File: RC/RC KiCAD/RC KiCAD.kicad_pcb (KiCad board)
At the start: 2 copper layers, 15 parts, among them U1 TL431AIDBZR

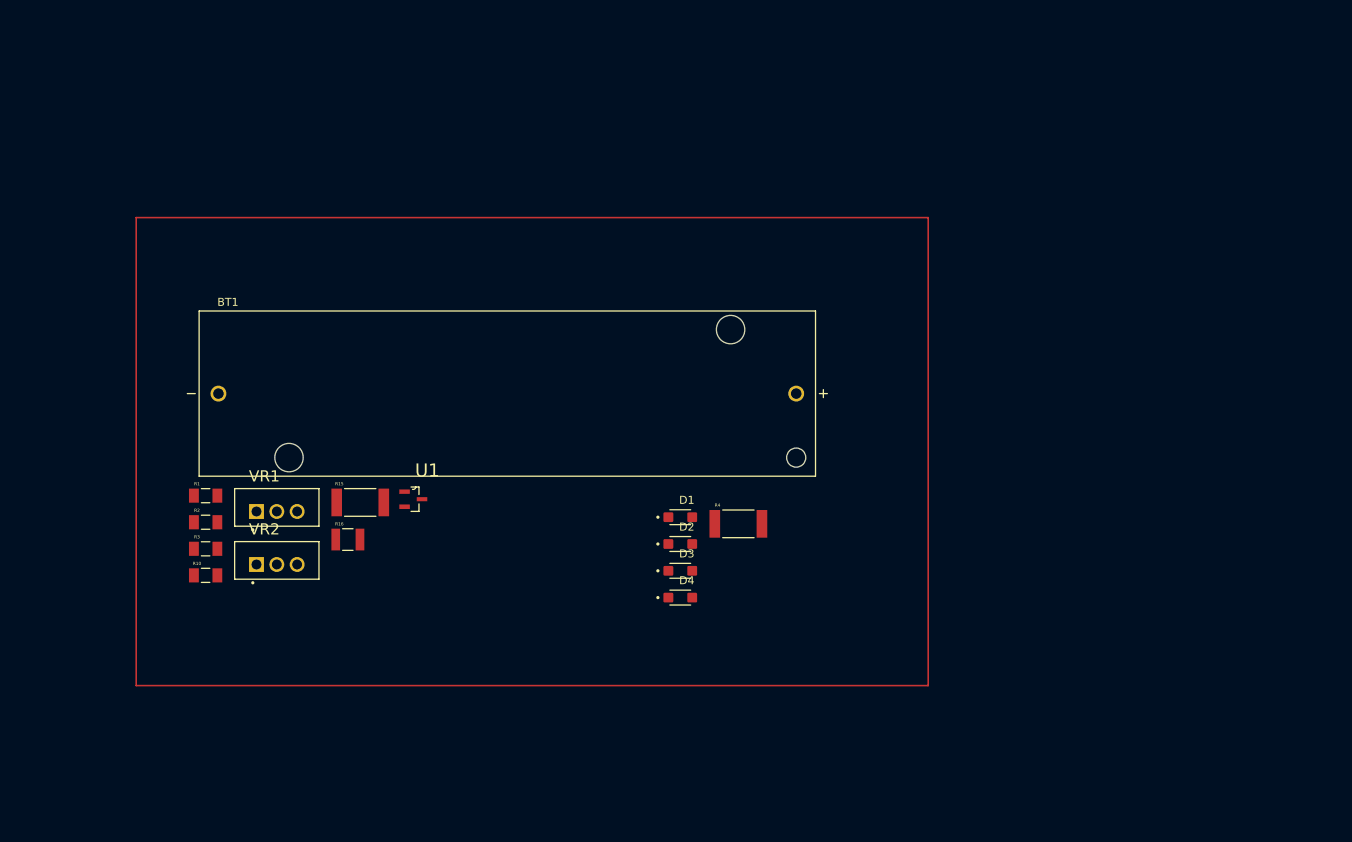
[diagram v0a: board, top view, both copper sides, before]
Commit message: Components Positioning
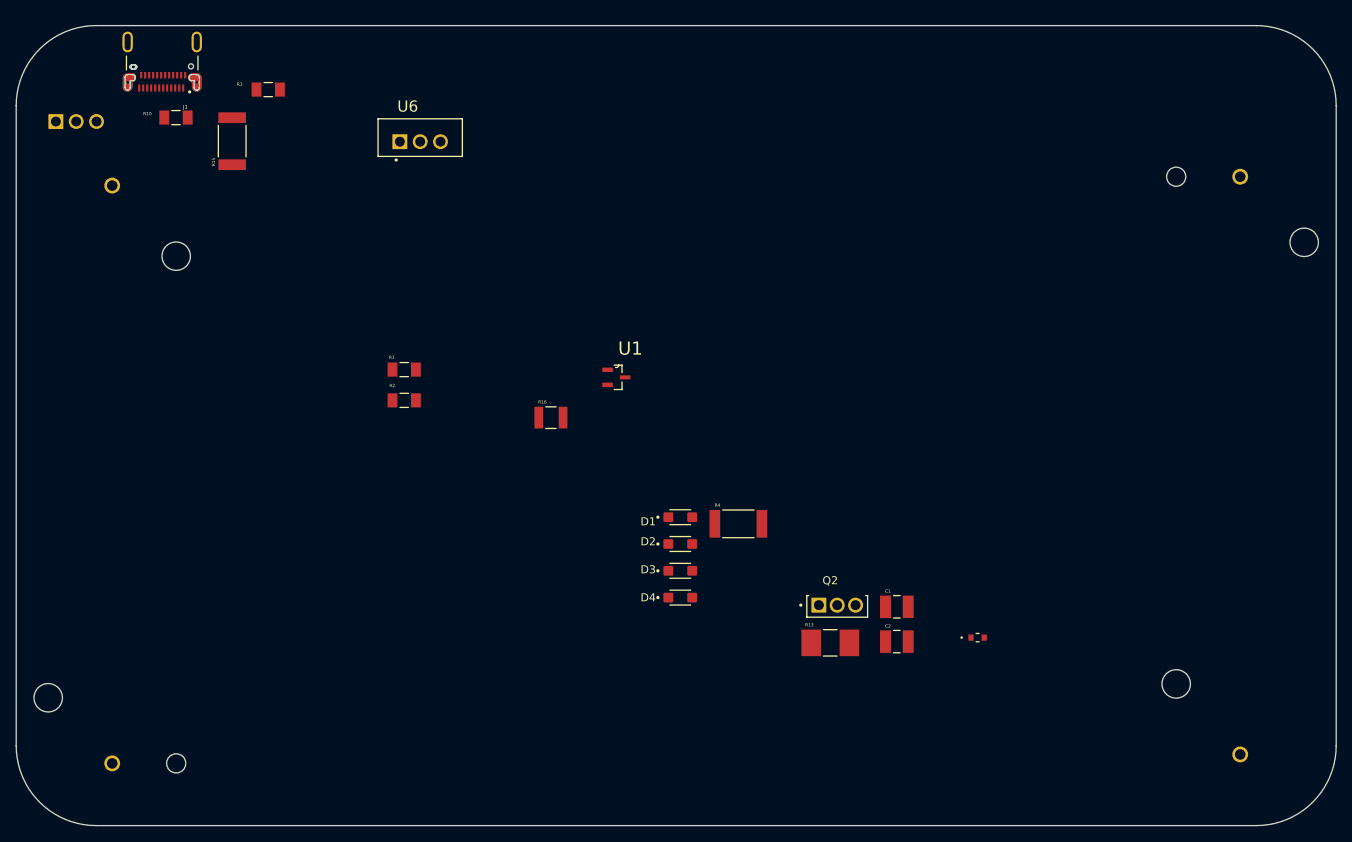
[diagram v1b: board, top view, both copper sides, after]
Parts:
- removed VR1, VR2: LM317T, LM317T:TO254P1054X470X1955-3
- added BT2: 1043P, Footprints:BAT_1043P, B.Cu at (182.5, 74.5)
- added C1: JMK325ABJ107MM-P, Footprints:CAPC3225X280N, F.Cu at (139.6, 92.2)
- added C2: JMK325ABJ107MM-P, Footprints:CAPC3225X280N, F.Cu at (139.6, 96.5)
- added J1: CX90B1-24P, Footprints:HRS_CX90B1-24P, F.Cu at (47.8, 21.6)
- added LED1: APT1608SGC, Footprints:LED_APT1608SGC_KNB, F.Cu at (149.7, 96.0)
- added Q2: BD140, Footprints:TO229P760X270X1364-3, F.Cu at (132.1, 92.1)
- added R13: CRM2512-FX-2R00ELF, Footprints:RESC6331X80N, F.Cu at (131.3, 96.7)
- added U12: LM317T, Footprints:TO254P1054X470X1955-3, B.Cu at (37.0, 32.0)
- added U6: LM317T, Footprints:TO254P1054X470X1955-3, F.Cu at (80.0, 33.5)
- BT1: moved to B.Cu
- moved R3 57.9 mm to (61.0, 27.5)
- moved R10 57.3 mm to (49.5, 31.0)
- moved BT1 50.4 mm to (41.5, 75.6), turned to -90 degrees
- moved R15 47.9 mm to (56.5, 33.9), turned to 90 degrees
- moved R16 29.6 mm to (96.3, 68.5)
- moved U1 29.6 mm to (104.5, 63.5)
- moved R1 29.4 mm to (78.0, 62.5)
- moved R2 29.1 mm to (78.0, 66.3)
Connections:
- BT1 pad N: GND -> Net-(BT1-PadN)
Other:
- board outline added: 165 x 100 mm

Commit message: New Components Added
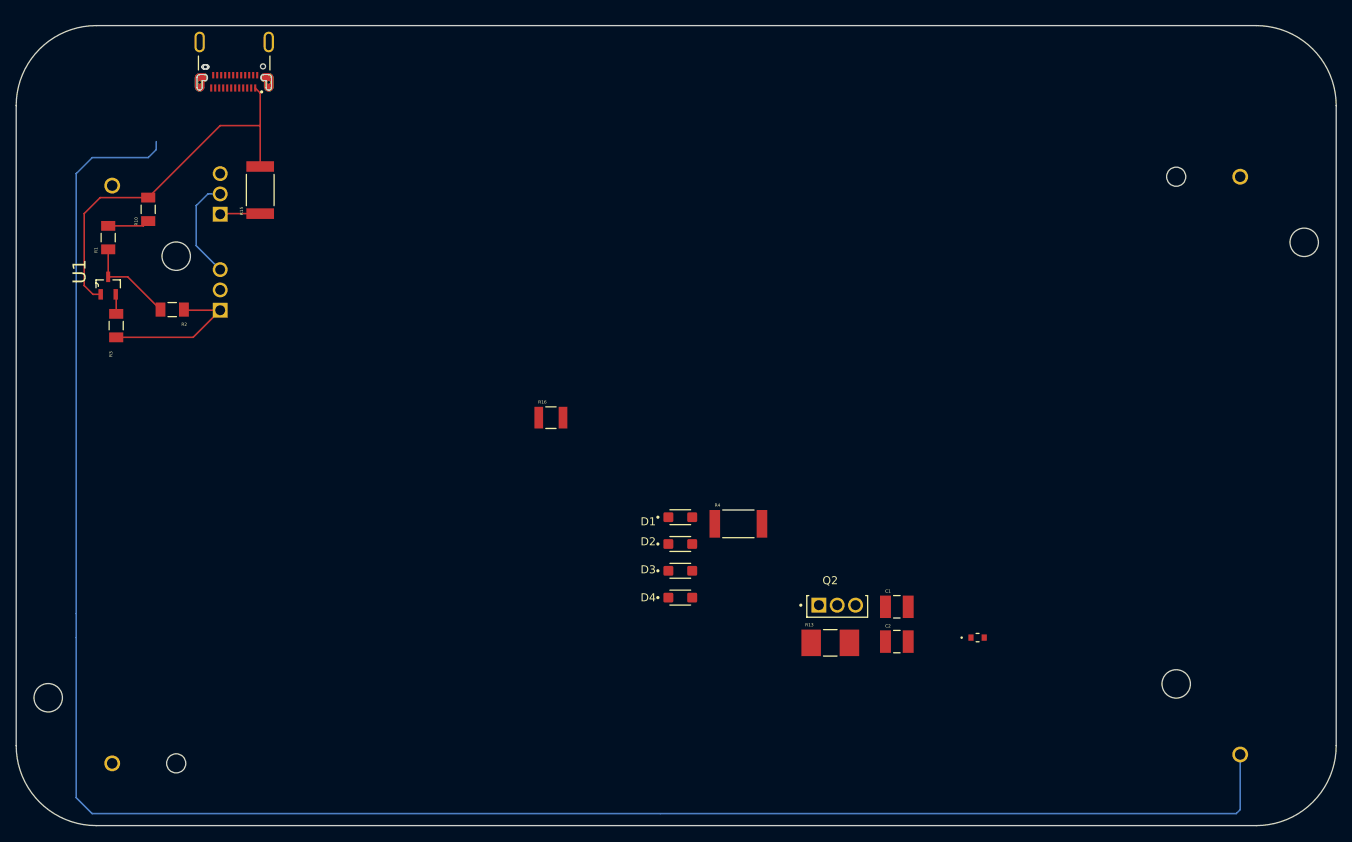
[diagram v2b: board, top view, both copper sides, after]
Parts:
- U6: moved to B.Cu
- moved U1 64.5 mm to (41.0, 52.0), turned to 90 degrees
- moved R1 40.5 mm to (41.0, 46.0), turned to 90 degrees
- moved R3 35.1 mm to (42.0, 57.0), turned to 90 degrees
- moved R2 31.1 mm to (49.0, 55.0), turned to 180 degrees
- moved U6 31.0 mm to (55.5, 52.5), turned to 90 degrees
- moved U12 20.4 mm to (55.5, 40.5), turned to 90 degrees
- moved R10 12.0 mm to (46.0, 42.5), turned to 90 degrees
- moved J1 9.00 mm to (56.8, 21.6)
- moved R15 7.04 mm to (60.0, 40.1)
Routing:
- net GND: track 0.00 -> 291.8 mm
- net Net-(U6-ADJ): track 0.00 -> 19.0 mm
- net Net-(U12-VOUT): track 0.00 -> 12.8 mm
- net AN: track 0.00 -> 11.7 mm
- net Net-(R1-Pad2): track 0.00 -> 5.25 mm
- net Net-(U12-ADJ): track 0.00 -> 5.03 mm
- net Net-(U1-CATHODE): track 0.00 -> 2.47 mm

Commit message: autosave: new components added
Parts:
- C1, Q2: moved to B.Cu
- J1: value CX90B1-24P -> USB4125-GF-A_REVA2; footprint Footprints:HRS_CX90B1-24P -> Footprints:GCT_USB4125-GF-A_REVA2
- moved LED1 110.7 mm to (68.2, 21.0), turned to 180 degrees
- moved C1 95.2 mm to (60.0, 39.9), turned to -90 degrees
- moved C2 90.1 mm to (64.0, 47.5), turned to 90 degrees
- moved D4 86.1 mm to (35.0, 53.5), turned to 180 degrees
- moved D3 86.0 mm to (35.0, 50.5)
- moved D2 85.8 mm to (35.0, 47.5), turned to 180 degrees
- moved D1 85.7 mm to (35.0, 44.5)
- moved Q2 82.1 mm to (54.8, 64.3), turned to -90 degrees
- moved R13 77.5 mm to (62.5, 61.0), turned to 180 degrees
- moved R4 59.5 mm to (62.5, 65.5)
- moved R16 42.0 mm to (60.0, 47.5), turned to 90 degrees
- moved J1 1.27 mm to (58.0, 21.8)
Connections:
- C1 pad 1: Net-(J1-VBUS_1A) -> Net-(J1-VBUS)
- J1 pad A12: unconnected-(J1-GND_2A-PadA12) -> GND
- J1 pad A5: unconnected-(J1-CC1-PadA5) -> USB D+
- J1 pad A9: unconnected-(J1-VBUS_2A-PadA9) -> Net-(J1-VBUS)
- J1 pad B12: unconnected-(J1-GND_2B-PadB12) -> GND
- J1 pad B5: unconnected-(J1-CC2-PadB5) -> USB D-
- J1 pad B9: unconnected-(J1-VBUS_2B-PadB9) -> Net-(J1-VBUS)
- U12 pad 3: Net-(J1-VBUS_1A) -> Net-(J1-VBUS)
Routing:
- net Net-(BT1-PadN): track 0.00 -> 161.1 mm
- net Net-(U6-ADJ): track 19.0 -> 88.3 mm, vias 0 -> 1
- net GND: track 291.8 -> 241.4 mm, vias 0 -> 3
- net Net-(D1-PadA): track 0.00 -> 47.5 mm, vias 0 -> 1
- net Net-(J1-VBUS): track 0.00 -> 31.5 mm
- net Net-(U1-CATHODE): track 2.47 -> 27.1 mm
- net Net-(U6-VOUT): track 0.00 -> 14.6 mm
- net Net-(U12-VOUT): track 12.8 -> 22.3 mm
- net Net-(D3-PadC): track 0.00 -> 3.00 mm
- net Net-(D2-PadC): track 0.00 -> 3.00 mm
- net Net-(D1-PadC): track 0.00 -> 3.00 mm
- net Net-(U12-ADJ): track 5.03 -> 8.00 mm
- net Net-(LED1-Pad1): track 0.00 -> 2.91 mm
- net (no net): track 0.00 -> 1.08 mm
- added copper zone on F.Cu, net GND
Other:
- copper layers 2 -> 4

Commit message: New BMS
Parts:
- added BOOT_SW1: PTS810_SJM_250_SMTR_LFS, Footprints:SW_PTS810_SJM_250_SMTR_LFS, F.Cu at (82.5, 44.5)
- added C3: 0.1uF, Capacitor_SMD:C_0805_2012Metric, F.Cu at (74.8, 62.2)
- added C4: 10uF, Capacitor_SMD:C_0805_2012Metric, F.Cu at (75.2, 78.3)
- added C5: 0.1uF, Capacitor_SMD:C_0805_2012Metric, F.Cu at (75.2, 81.3)
- added C6: 0.1uF, Capacitor_SMD:C_0805_2012Metric, F.Cu at (75.2, 84.3)
- added C7: 10uF, Capacitor_SMD:C_0805_2012Metric, F.Cu at (113.0, 60.3)
- added C8: 10uF, Capacitor_SMD:C_0805_2012Metric, F.Cu at (113.0, 63.3)
- added D5: WS2812B, LED_SMD:LED_WS2812B_PLCC4_5.0x5.0mm_P3.2mm, F.Cu at (82.9, 59.8)
- added D6: LED, LED_SMD:LED_0603_1608Metric, F.Cu at (137.5, 48.7)
- added H1: MountingHole_Pad, MountingHole:MountingHole_2.2mm_M2_Pad, F.Cu at (38.4, 26.7)
- added H2: MountingHole_Pad, MountingHole:MountingHole_2.2mm_M2_Pad, F.Cu at (184.2, 26.2)
- added H3: MountingHole_Pad, MountingHole:MountingHole_2.2mm_M2_Pad, F.Cu at (69.6, 60.1)
- added H4: MountingHole_Pad, MountingHole:MountingHole_2.2mm_M2_Pad, F.Cu at (165.8, 108.3)
- added J2: ~, Footprints:CON_524373071_MOL, F.Cu at (134.7, 101.0)
- added LS1: CEM-1206S, Footprints:CUI_CEM-1206S, B.Cu at (159.9, 61.1)
- added R11: 5.1k, Resistor_SMD:R_1206_3216Metric, F.Cu at (108.0, 67.0)
- added R5: 5.1k, Resistor_SMD:R_0805_2012Metric, F.Cu at (94.6, 93.6)
- added R6: 5.1k, Resistor_SMD:R_0805_2012Metric, F.Cu at (94.6, 96.5)
- added R7: 10k, Resistor_SMD:R_0805_2012Metric, F.Cu at (88.1, 43.6)
- added R8: 1M, Resistor_SMD:R_1206_3216Metric, F.Cu at (108.0, 60.4)
- added R9: 200k, Resistor_SMD:R_1206_3216Metric, F.Cu at (108.0, 63.7)
- added RESET_SW1: PTS810_SJM_250_SMTR_LFS, Footprints:SW_PTS810_SJM_250_SMTR_LFS, F.Cu at (82.5, 49.3)
- added S1: 400BWMSP1R2BLKSM6QE, Footprints:SW_400BWMSP1R2BLKSM6QE, B.Cu at (88.4, 29.1)
- added U2: D3V3XA4B10LP, Package_DFN_QFN:Diodes_UDFN-10_1.0x2.5mm_P0.5mm, F.Cu at (117.7, 43.7)
- added U3: ESP32-S3-WROOM-2-N32R8V, Footprints:XCVR_ESP32-S3-WROOM-2-N32R8V, F.Cu at (140.8, 32.9)
- added U4: TLV75801PDBV, Package_TO_SOT_SMD:SOT-23-5, F.Cu at (106.4, 27.9)
- C1, Q2, U12, U6: moved to F.Cu
- D1, D2, D3, D4: footprint DSS14UTR:SODFL3618X110N -> Footprints:SODFL3618X110N
- J1: value USB4125-GF-A_REVA2 -> USB4085; footprint Footprints:GCT_USB4125-GF-A_REVA2 -> Footprints:GCT_USB4085-GF-A_REVB
- R1, R10, R2: footprint RMCF1206FT20R0:RESC3216X70N -> Footprints:RESC3216X70N
- R15: footprint RMCF2512JT3K30:RESC6332X70N -> Footprints:RESC3216X70N
- R16: footprint CRCW12101K40FKEA:RESC3225X60N -> Footprints:RESC3225X60N
- R3: footprint RMCF1206FT1K00:RESC3216X70N -> Footprints:RESC3216X70N
- R4: footprint RMCF2512JT330R:RESC6332X70N -> Footprints:RESC6332X70N
- U1: footprint TL431AIDBZR:SOT95P237X112-3N -> Footprints:SOT95P237X112-3N
- moved U1 76.8 mm to (108.8, 88.0), turned to 0 degrees
- moved R10 72.9 mm to (102.8, 88.0), turned to 0 degrees
- moved R1 69.7 mm to (103.8, 76.2), turned to 0 degrees
- moved R15 67.6 mm to (103.7, 91.6), turned to 0 degrees
- moved R3 66.3 mm to (102.3, 84.3), turned to 0 degrees
- moved R16 61.3 mm to (109.4, 83.8), turned to 0 degrees
- moved R2 58.6 mm to (101.8, 80.3), turned to 0 degrees
- moved D4 58.2 mm to (64.6, 103.6), turned to 0 degrees
- moved D3 57.9 mm to (64.6, 100.2)
- moved D2 57.6 mm to (64.6, 96.9), turned to 0 degrees
- moved D1 57.3 mm to (64.6, 93.6)
- moved R4 54.9 mm to (116.4, 75.8)
- moved Q2 37.9 mm to (83.9, 40.0), turned to 0 degrees
- moved R13 21.7 mm to (83.1, 54.1), turned to 0 degrees
- moved U6 20.7 mm to (72.6, 41.0), turned to 0 degrees
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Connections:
- net AN renamed /ANODE
- J1 pad A5: USB D+ -> Net-(J1-CC1)
- J1 pad B5: USB D- -> Net-(J1-CC2)
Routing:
- net GND: track 241.4 -> 2.92 mm, vias 3 -> 0
- net Net-(BT1-PadN): track 161.1 -> 0.00 mm
- net Net-(U6-ADJ): track 88.3 -> 0.00 mm, vias 1 -> 0
- net Net-(D1-PadA): track 47.5 -> 0.00 mm, vias 1 -> 0
- net Net-(J1-VBUS): track 31.5 -> 3.16 mm
- net Net-(U1-CATHODE): track 27.1 -> 0.00 mm
- net Net-(U12-VOUT): track 22.3 -> 0.00 mm
- net Net-(U6-VOUT): track 14.6 -> 0.00 mm
- net /ANODE: track 11.7 -> 0.00 mm
- net Net-(U12-ADJ): track 8.00 -> 0.00 mm
- net Net-(R1-Pad2): track 5.25 -> 0.00 mm
- net Net-(D3-PadC): track 3.00 -> 0.00 mm
- net Net-(D2-PadC): track 3.00 -> 0.00 mm
- net Net-(D1-PadC): track 3.00 -> 0.00 mm
- net Net-(LED1-Pad1): track 2.91 -> 0.00 mm
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- removed copper zone on F.Cu, net GND
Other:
- copper layers 4 -> 2
